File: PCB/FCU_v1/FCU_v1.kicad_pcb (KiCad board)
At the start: 2 copper layers, 57.6 x 60.8 mm, 106 parts, among them J1 Conn_01x04_Pin, J10 Conn_01x04_Pin, J2 USB_B_Micro, J3 Conn_01x05_Pin, J4 Conn_Coaxial_Small, J5 Conn_01x04_Pin, J6 Conn_01x04_Pin, J7 Conn_01x04_Pin, J8 Conn_01x04_Pin, J9 Conn_01x04_Pin, U1 TPS62132, U10 SN65HVD232, U11 STM32G473RETx, U3 TLV75533PDYDR, U4 BMI088, U5 LIS2MDL, U6 LPS22HH, U7 W25Q64JV, U8 USBLC6-2SC6, U9 MAX-M10M-20B, Y2 16MHz

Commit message: Add FCU block diagram and update PCB layout
Added FCU.drawio block diagram and new STM/STM2 IOC files. Updated FCU_v1.kicad_pcb with component position changes and connector orientation. Added a new backup ZIP for FCU_v1.
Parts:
- moved C11 118.3 mm to (113.6, 84.5)
- moved C12 118.3 mm to (113.6, 87.5)
- moved FB1 114.3 mm to (130.0, 86.8), turned to 180 degrees
- moved C14 108.2 mm to (129.0, 84.0), turned to 90 degrees
- moved Y2 105.8 mm to (139.1, 83.4)
- moved C13 100.4 mm to (131.1, 84.0), turned to 90 degrees
- moved C9 96.5 mm to (135.2, 77.4), turned to 90 degrees
- moved C8 93.2 mm to (134.1, 90.2), turned to 180 degrees
- moved C16 93.1 mm to (143.4, 83.3)
- moved C41 93.1 mm to (143.4, 86.4)
- moved C7 80.7 mm to (147.4, 91.3), turned to -90 degrees
- moved C5 78.6 mm to (148.2, 76.3)
- moved C6 78.6 mm to (148.2, 78.3)
- moved J10 26.2 mm to (155.5, 103.9), turned to 90 degrees
- moved J9 24.7 mm to (102.1, 96.4), turned to -90 degrees
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
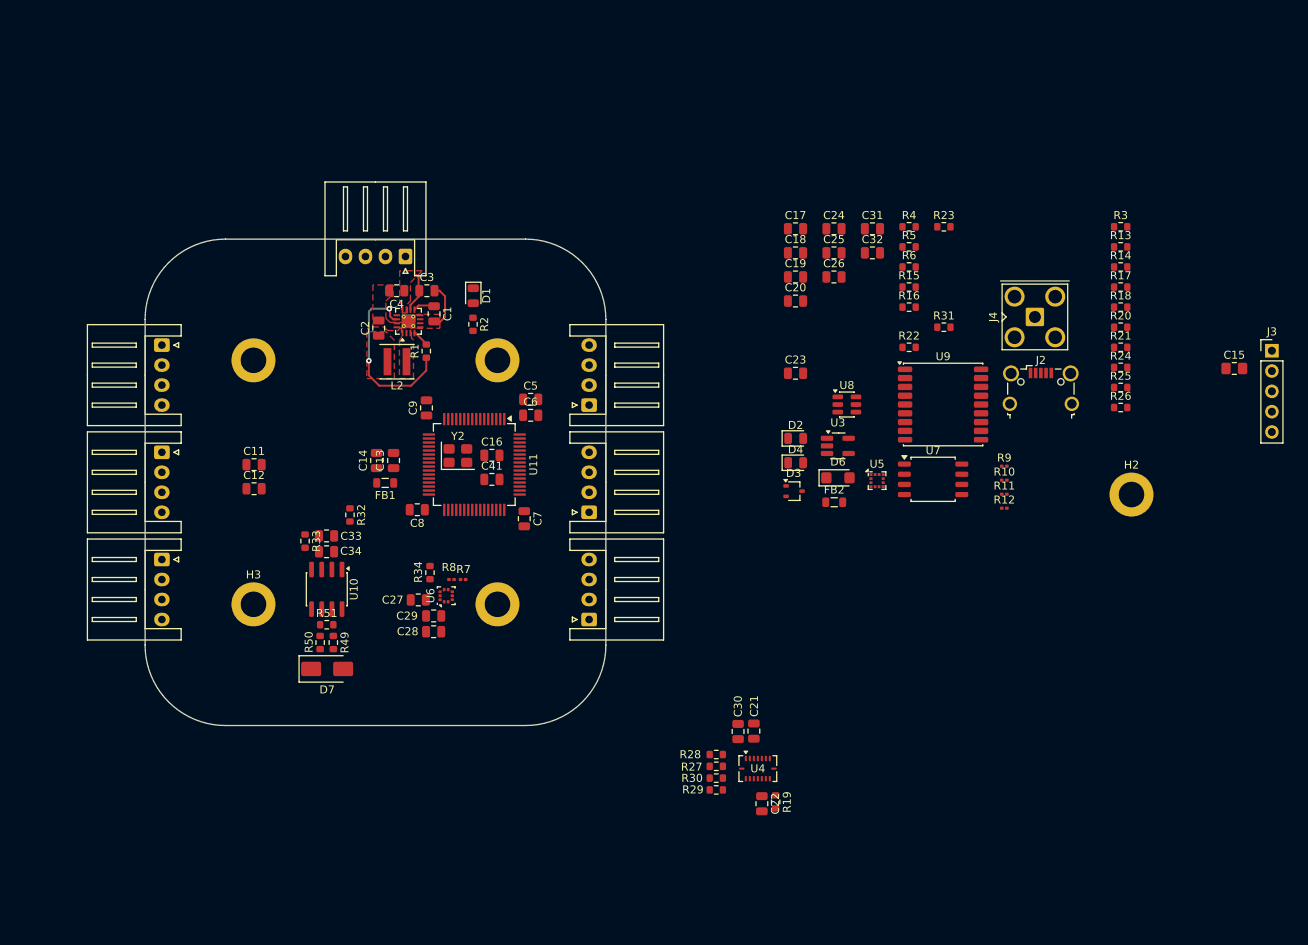
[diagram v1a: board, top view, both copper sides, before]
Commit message: Update FCU_v1 PCB and add new resistors
Reworked net assignments and added new nets in FCU_v1.kicad_pcb. Added and repositioned resistors R23 and R28, and updated footprints and net connections. Also updated several backup files and made minor schematic changes in MCU.kicad_sch and PERIPHERALS.kicad_sch.
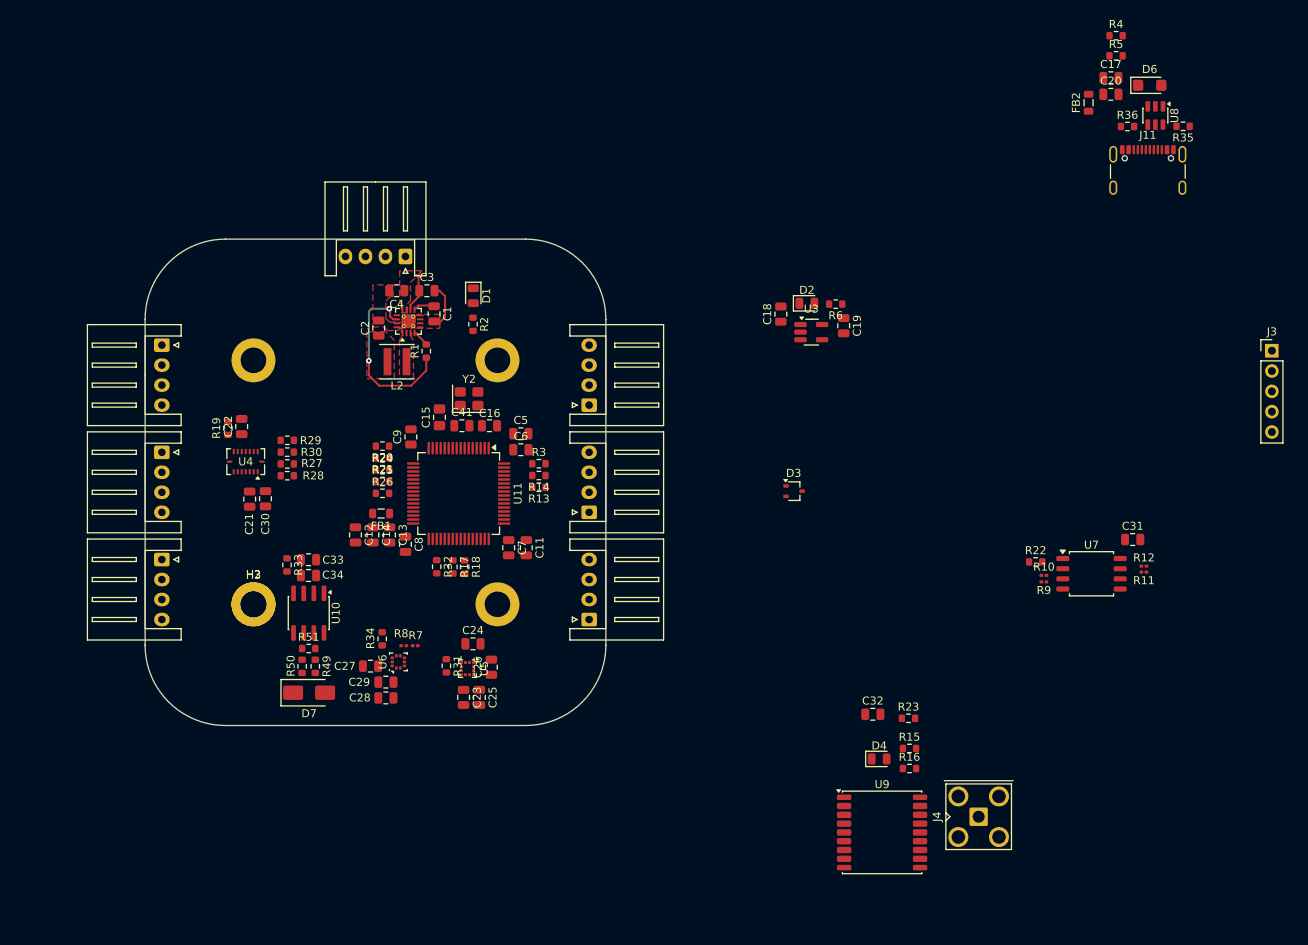
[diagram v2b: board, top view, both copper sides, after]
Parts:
- removed J2: USB_B_Micro, Connector_USB:USB_Micro-B_Wuerth_629105150521_CircularHoles
- added J11: USB_C_Receptacle_USB2.0_16P, Connector_USB:USB_C_Receptacle_GCT_USB4105-xx-A_16P_TopMnt_Horizontal, F.Cu at (225.4, 48.8)
- added R35: 5k1, Resistor_SMD:R_0603_1608Metric, F.Cu at (229.8, 42.2)
- added R36: 5k1, Resistor_SMD:R_0603_1608Metric, F.Cu at (222.8, 42.2)
- moved H2 110.6 mm to (113.6, 102.0)
- moved C15 99.5 mm to (136.8, 78.6), turned to 90 degrees
- moved R20 93.5 mm to (129.7, 82.2), turned to 180 degrees
- moved R21 93.3 mm to (129.7, 83.7), turned to 180 degrees
- moved R24 93.2 mm to (129.7, 85.2)
- moved R25 93.0 mm to (129.7, 86.6)
- moved R26 92.9 mm to (129.7, 88.1)
- moved R17 90.5 mm to (138.5, 97.3), turned to -90 degrees
- moved R18 88.2 mm to (140.0, 97.3), turned to -90 degrees
- moved R19 82.9 mm to (110.4, 80.0), turned to -90 degrees
- moved C22 80.3 mm to (112.1, 79.8), turned to 90 degrees
- moved R13 78.7 mm to (149.2, 87.3), turned to 180 degrees
- moved R3 78.5 mm to (149.2, 84.4)
- moved R14 77.3 mm to (149.2, 85.9), turned to 180 degrees
- moved R31 75.2 mm to (137.7, 109.7), turned to -90 degrees
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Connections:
- net Net-(D6-A1) renamed /PERIPHERALS/USB_VBUS
- C16 pad 1: Net-(C16-Pad1) -> GND
- C18 pad 2: Net-(C18-Pad2) -> GND
- C19 pad 2: Net-(C18-Pad2) -> GND
- C41 pad 1: Net-(C16-Pad1) -> GND

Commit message: Adjust PCB footprint positions and metadata
Add three FCU_v1 backup archives and apply multiple PCB layout fixes: reposition and reorient many footprints (resistors, capacitors, inductors, diodes, SOT-23, LQFP, LGA, etc.), update pad orientation/rotation entries, and correct numerous fp_line coordinates and UUIDs. Also include small updates to project/prl and PERIPHERALS schematic references. These changes refine component placement and silkscreen/fabrication outlines for the FCU_v1 board.
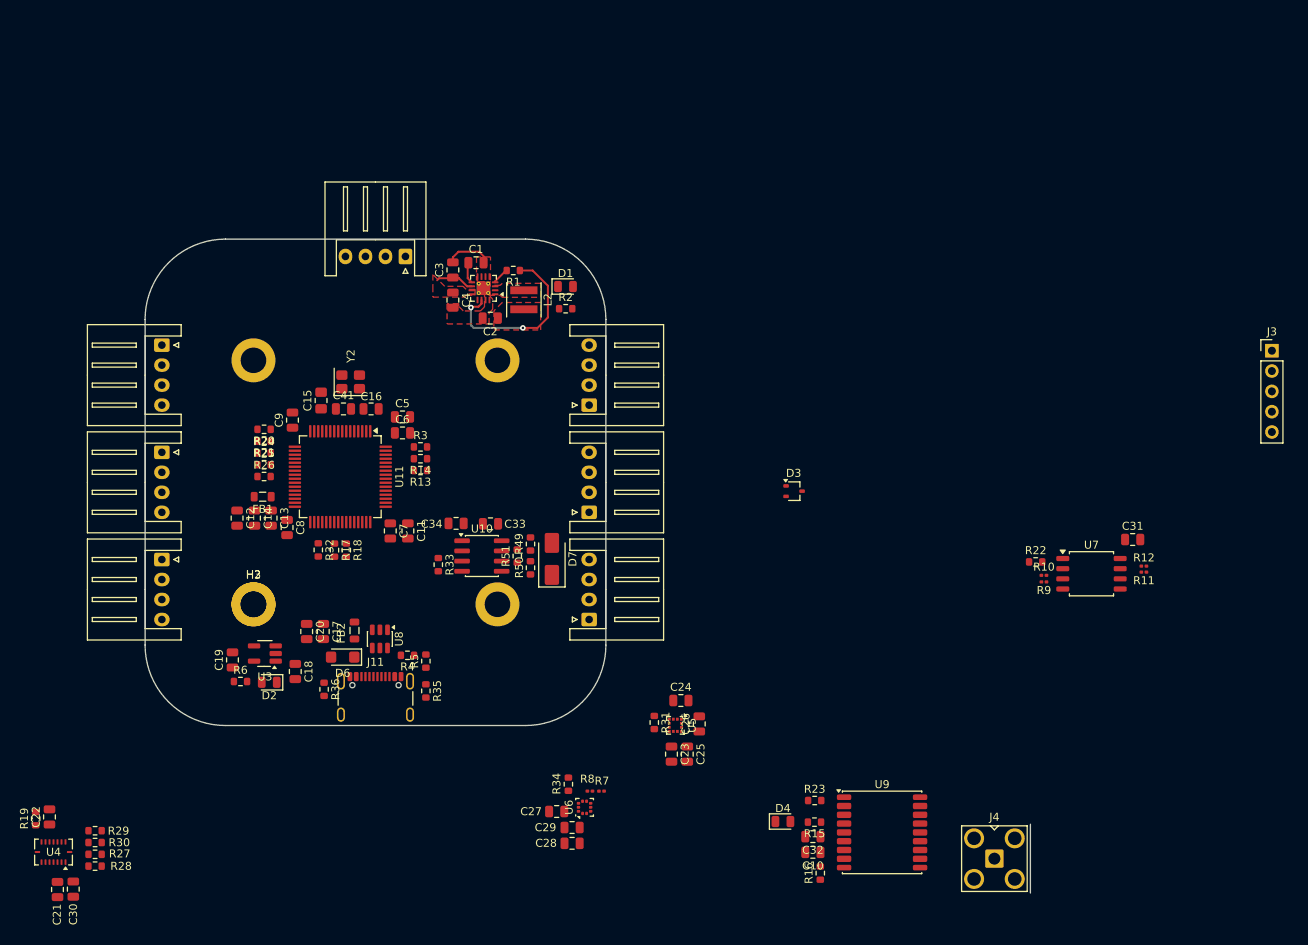
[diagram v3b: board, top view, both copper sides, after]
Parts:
- added C10: 100n, Capacitor_SMD:C_0805_2012Metric, F.Cu at (183.5, 133.0)
- moved D6 123.6 mm to (124.7, 108.6), turned to 180 degrees
- moved R36 122.6 mm to (122.4, 112.6), turned to -90 degrees
- moved C20 120.9 mm to (120.2, 105.4), turned to -90 degrees
- moved C17 120.4 mm to (122.3, 105.4), turned to -90 degrees
- moved R35 118.1 mm to (135.1, 112.8), turned to -90 degrees
- moved R4 117.7 mm to (132.8, 108.3), turned to 180 degrees
- moved U8 117.0 mm to (129.4, 106.3)
- moved J11 116.9 mm to (128.8, 114.7)
- moved R5 114.8 mm to (135.1, 109.1), turned to 90 degrees
- moved FB2 113.0 mm to (126.2, 105.2)
- moved R6 88.1 mm to (112.0, 111.6), turned to 0 degrees
- moved C19 87.1 mm to (111.0, 108.9), turned to 90 degrees
- moved D2 82.2 mm to (115.5, 111.7), turned to 180 degrees
- moved U3 79.2 mm to (115.0, 108.1), turned to 180 degrees
- moved C18 75.4 mm to (118.8, 110.4), turned to -90 degrees
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
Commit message: Added next version v2
Added notes for next version with what needs to be improved or completely fixed. Notes in schematic file
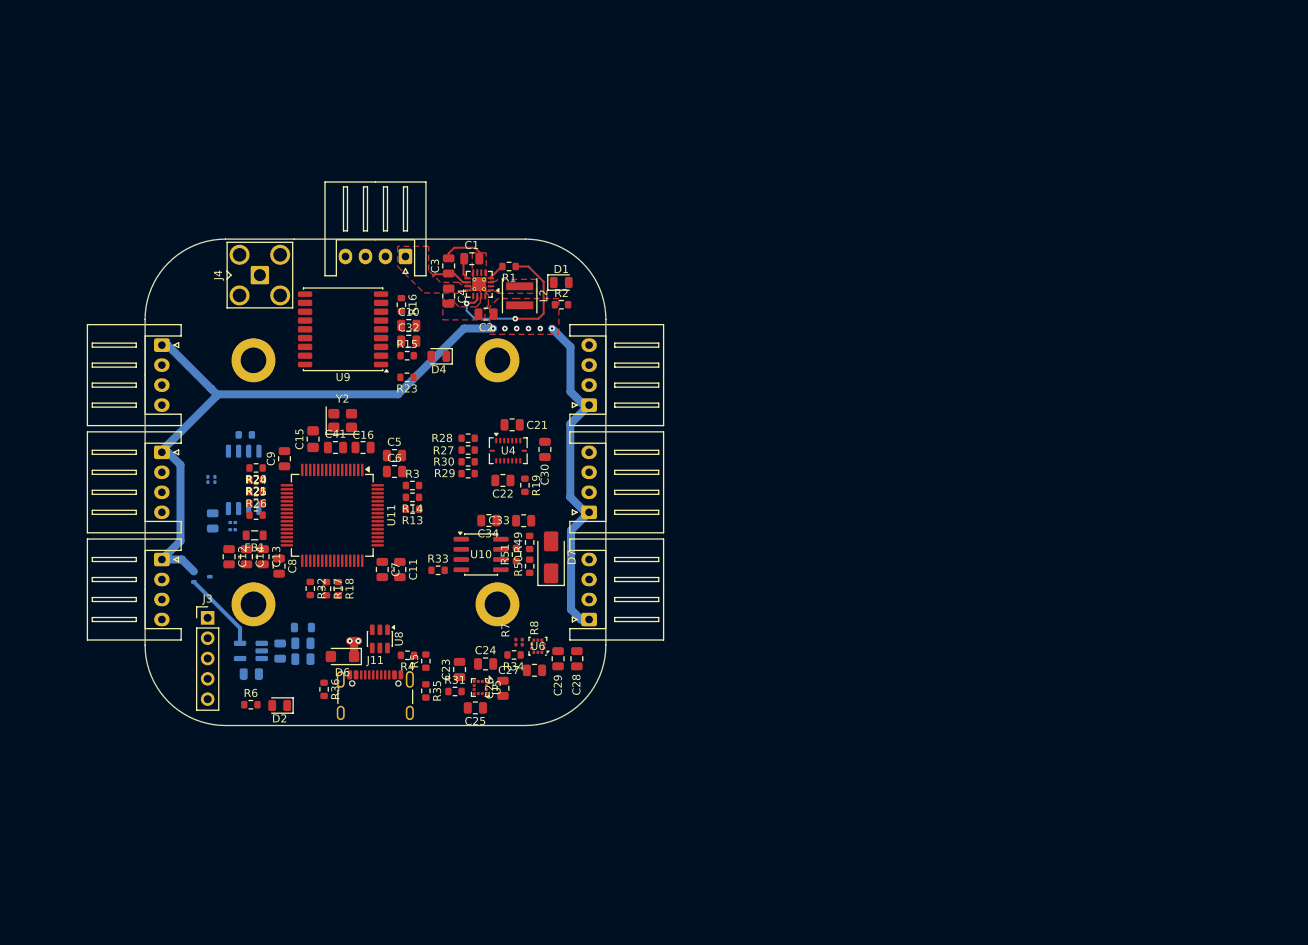
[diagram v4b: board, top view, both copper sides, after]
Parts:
- removed the H3 at (113.6, 102.0)
- C17, C18, C19, C20, C31, D3, FB2, R10, R11, R12, R22, R9, U3, U7: moved to B.Cu
- moved J3 137.2 mm to (107.8, 103.7)
- moved J4 117.3 mm to (114.4, 60.8), turned to 0 degrees
- moved C31 115.0 mm to (108.5, 91.5), turned to -90 degrees
- moved R12 114.0 mm to (111.0, 91.8), turned to 180 degrees
- moved R11 114.0 mm to (111.0, 92.7), turned to 0 degrees
- moved U7 106.6 mm to (112.3, 86.4), turned to -90 degrees
- moved R10 105.2 mm to (107.9, 86.4), turned to 90 degrees
- moved R9 104.4 mm to (108.8, 86.4), turned to -90 degrees
- moved R22 100.1 mm to (112.5, 80.8), turned to 180 degrees
- moved U9 92.2 mm to (124.8, 67.6), turned to 180 degrees
- moved R16 88.3 mm to (132.1, 64.5), turned to -90 degrees
- moved C10 83.0 mm to (133.0, 67.1), turned to 0 degrees
- moved C21 81.3 mm to (145.9, 79.5), turned to 0 degrees
- moved C30 80.6 mm to (150.0, 82.6)
- moved C32 79.9 mm to (133.0, 69.1), turned to 0 degrees
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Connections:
- net Net-(U11-PB0) renamed /MCU/CS_MEM
- net Net-(U11-PB5) renamed /MCU/GNSS_Rst
- net Net-(U11-PB6) renamed /MCU/GNSS_Tx
- net Net-(U11-PC4) renamed /MCU/CSB_ACCE
- net Net-(U11-PC5) renamed /MCU/CSB_GYR
- net Net-(U5-C1) renamed /PERIPHERALS/MAG_C1
- D3 pad 1: 3V3 -> VBUS_3V3
- D3 pad 2: VBUS_3V3 -> 3V3
- R20 pad 1: Net-(U11-PA5) -> SPI_SCK
- R21 pad 1: Net-(U11-PA7) -> SPI_MOSI
- R31 pad 2: Net-(U5-DRDY) -> MAG_INT
- U11 pad 19: Net-(U11-PA5) -> SPI_SCK
- U11 pad 21: Net-(U11-PA7) -> SPI_MOSI
- U5 pad 7: Net-(U5-DRDY) -> MAG_INT
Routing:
- net 3V3: track 22.7 -> 142.5 mm, vias 2 -> 8
- net VBUS_3V3: track 0.00 -> 10.1 mm
- net /PERIPHERALS/USB_VBUS: track 0.00 -> 3.00 mm, vias 0 -> 2
- added copper zone on In1.Cu, net GND
- added copper zone on In2.Cu, net GND
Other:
- outline, holes or cut-outs redrawn
- copper layers 2 -> 4

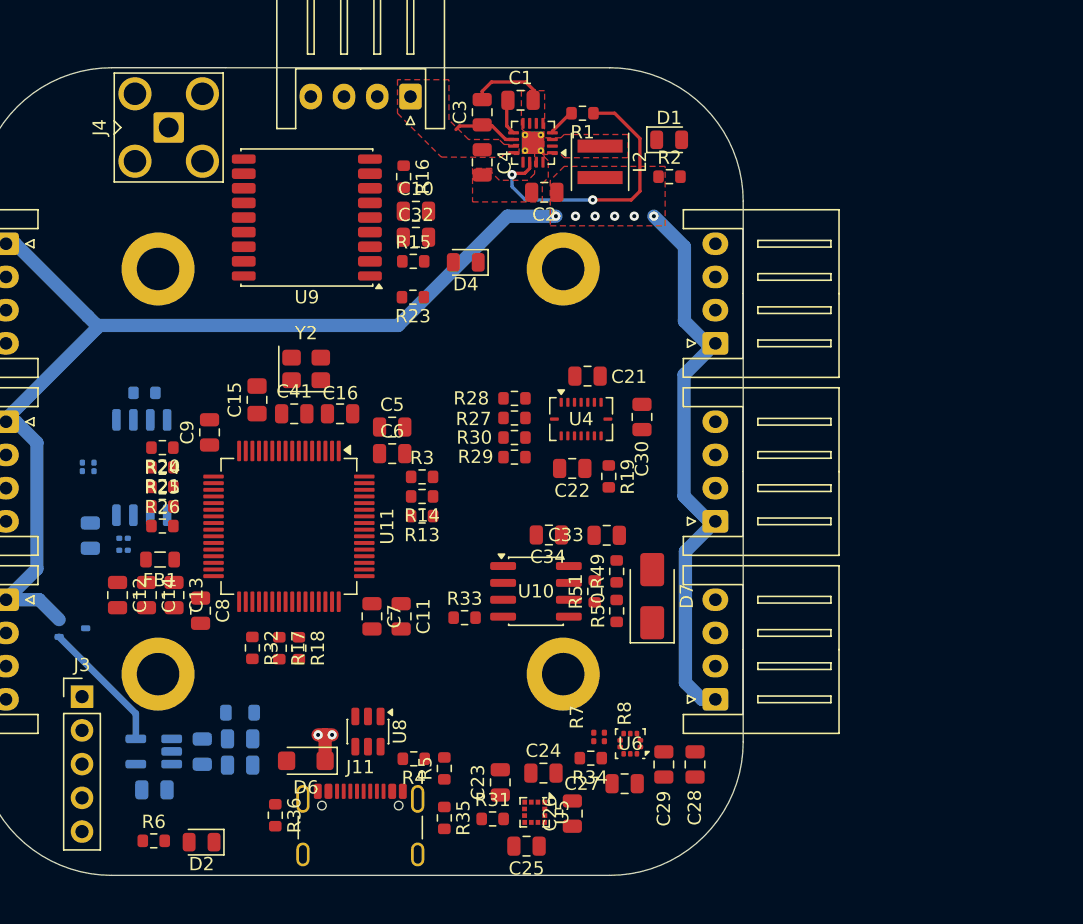
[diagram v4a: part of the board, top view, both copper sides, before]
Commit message: Update PCB footprints, positions and backups
Remove old FCU_v1 backup zips and add new timestamped backups. Apply extensive edits to PCB/FCU_v1.kicad_pcb: reposition and rotate multiple footprints, fix pad orientations, update silkscreen/fab/crtyd outlines and UUIDs, change some net mappings and sheet/path references, and replace a resistor footprint with a SOT-23-6 ESD device (USBLC6) including updated properties and datasheet. Update related project/schematic files (FCU_v1.kicad_prl, FCU_v1.kicad_sch, PERIPHERALS.kicad_sch) to reflect these changes.
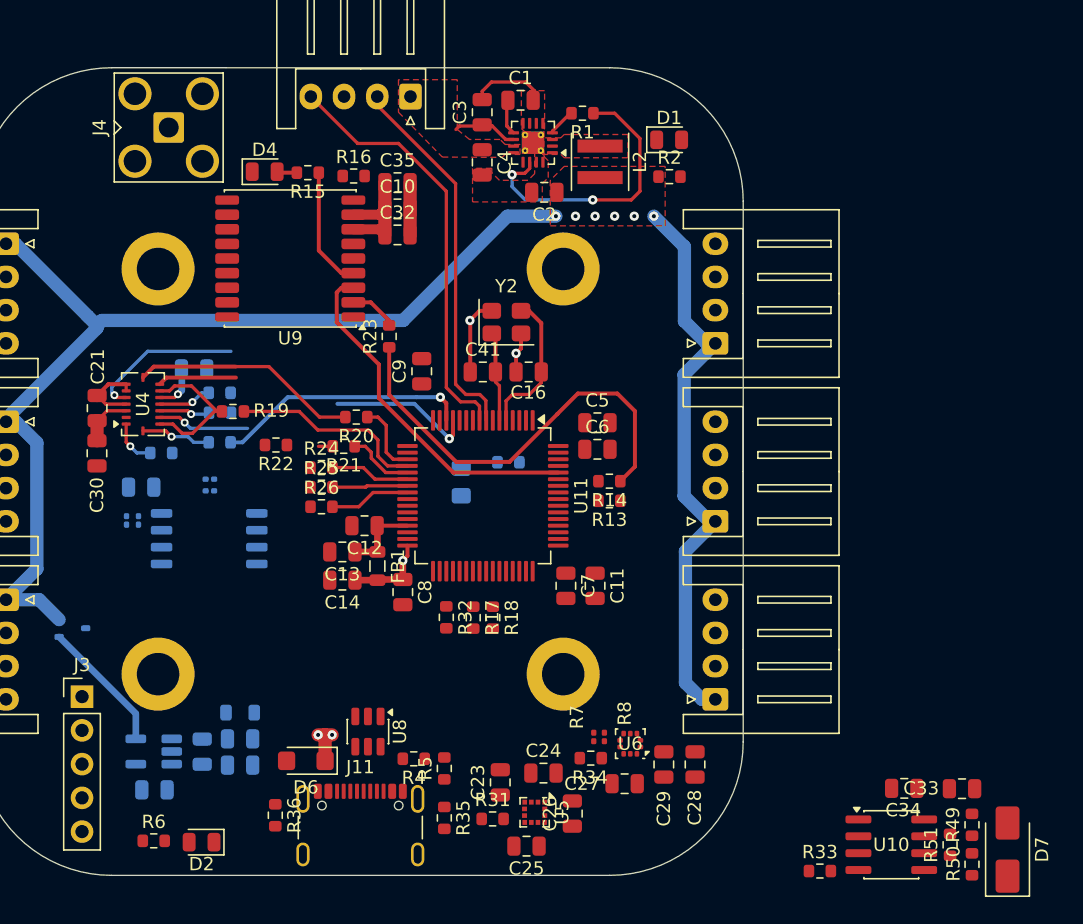
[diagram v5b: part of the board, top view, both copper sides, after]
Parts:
- added C35: 4u7-10u, Capacitor_SMD:C_0805_2012Metric, F.Cu at (131.6, 65.0)
- C15, C22, R27, R28, R29, R3, R30: moved to B.Cu
- R22: moved to F.Cu
- moved C30 41.1 mm to (109.0, 85.3)
- moved C21 37.0 mm to (109.0, 82.0), turned to 90 degrees
- moved U4 33.0 mm to (112.4, 81.7), turned to 90 degrees
- moved C34 32.9 mm to (169.8, 110.6)
- moved D7 32.9 mm to (177.5, 115.2)
- moved R33 32.9 mm to (163.4, 116.8)
- moved R50 32.9 mm to (174.8, 116.3)
- moved R51 32.9 mm to (173.2, 114.8)
- moved C33 32.9 mm to (174.1, 110.6)
- moved R49 32.9 mm to (174.8, 113.3)
- moved U10 32.9 mm to (168.8, 114.8)
- moved C22 29.4 mm to (116.3, 79.0), turned to 0 degrees
- moved R19 28.7 mm to (119.2, 82.2), turned to 180 degrees
- moved R28 26.9 mm to (113.8, 85.3), turned to 180 degrees
- moved R29 22.7 mm to (118.2, 80.8), turned to 180 degrees
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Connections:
- J1 pad 2: BAT_CURR -> BAT_VOL
- J1 pad 4: BAT_VOL -> BAT_CURR
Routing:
- net GNSS_TX: track 0.00 -> 32.6 mm
- net BAT_CURR: track 0.00 -> 32.1 mm
- net BAT_VOL: track 0.00 -> 28.4 mm
- net GNSS_RX: track 0.00 -> 26.5 mm
- net 3V3_FCU: track 0.00 -> 22.9 mm, vias 0 -> 2
- net SPI_SCK: track 0.00 -> 22.7 mm
- net INT1_ACCEL: track 0.00 -> 19.1 mm, vias 0 -> 1
- net GND: track 5.76 -> 24.6 mm, vias 0 -> 2
- net SPI_MISO: track 0.00 -> 15.5 mm
- net SPI_MOSI: track 0.00 -> 12.1 mm
- net CSB_GYRO: track 0.00 -> 11.7 mm, vias 0 -> 1
- net Net-(U4-SDO1): track 0.00 -> 11.3 mm
- net OSC_IN: track 0.00 -> 11.1 mm
- net INT2_ACCEL: track 0.00 -> 11.0 mm, vias 0 -> 1
- net Net-(U9-TIMEPULSE): track 0.00 -> 9.17 mm
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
